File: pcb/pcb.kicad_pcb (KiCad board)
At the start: 2 copper layers, 56 x 58 mm, 20 parts, among them J1 Conn_01x03_Pin, J2 Screw_Terminal_01x06, J3 Barrel_Jack_Switch, J5 DE9_Plug, U1 74LS165, U2 LM7805_TO220

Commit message: New PDB files
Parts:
- removed J5: DE9_Plug, Connector_Dsub:DSUB-9_Female_Horizontal_P2.77x2.84mm_EdgePinOffset7.70mm_Housed_MountingHolesOffset9.12mm
- added J4: DE9_Plug_MountingHoles, Connector_Dsub:DSUB-9_Female_Horizontal_P2.77x2.84mm_EdgePinOffset7.70mm_Housed_MountingHolesOffset9.12mm, F.Cu at (190.7, 79.5)
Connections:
- J2 pad 4: VIDEO -> V_SYNC
- J2 pad 5: V_SYNC -> VIDEO
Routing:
- net VIDEO: track 29.0 -> 31.5 mm
- net PARALLEL_LOAD: track 34.3 -> 35.4 mm
- net V_SYNC: track 42.1 -> 43.1 mm
- net +5V: track 91.8 -> 91.2 mm
- net GND: vias 13 -> 18

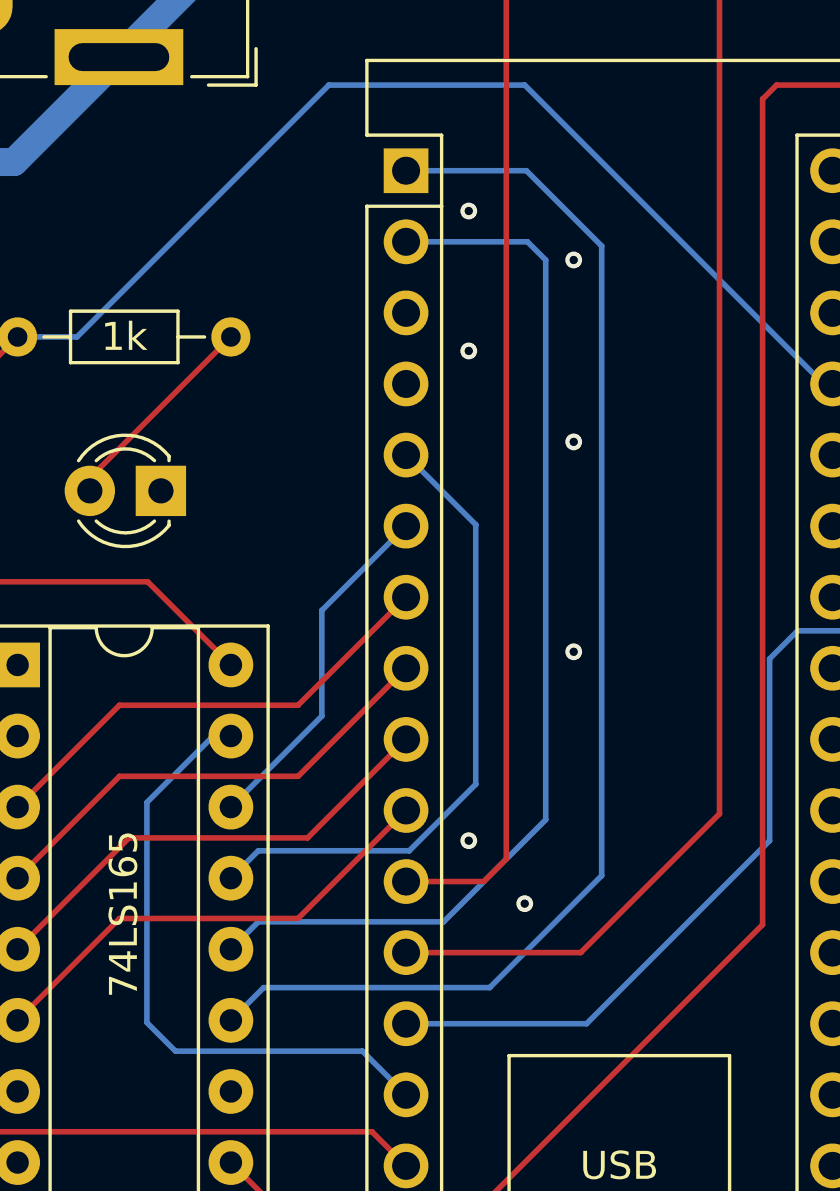
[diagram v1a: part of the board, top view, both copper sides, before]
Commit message: Fix backwards data lines
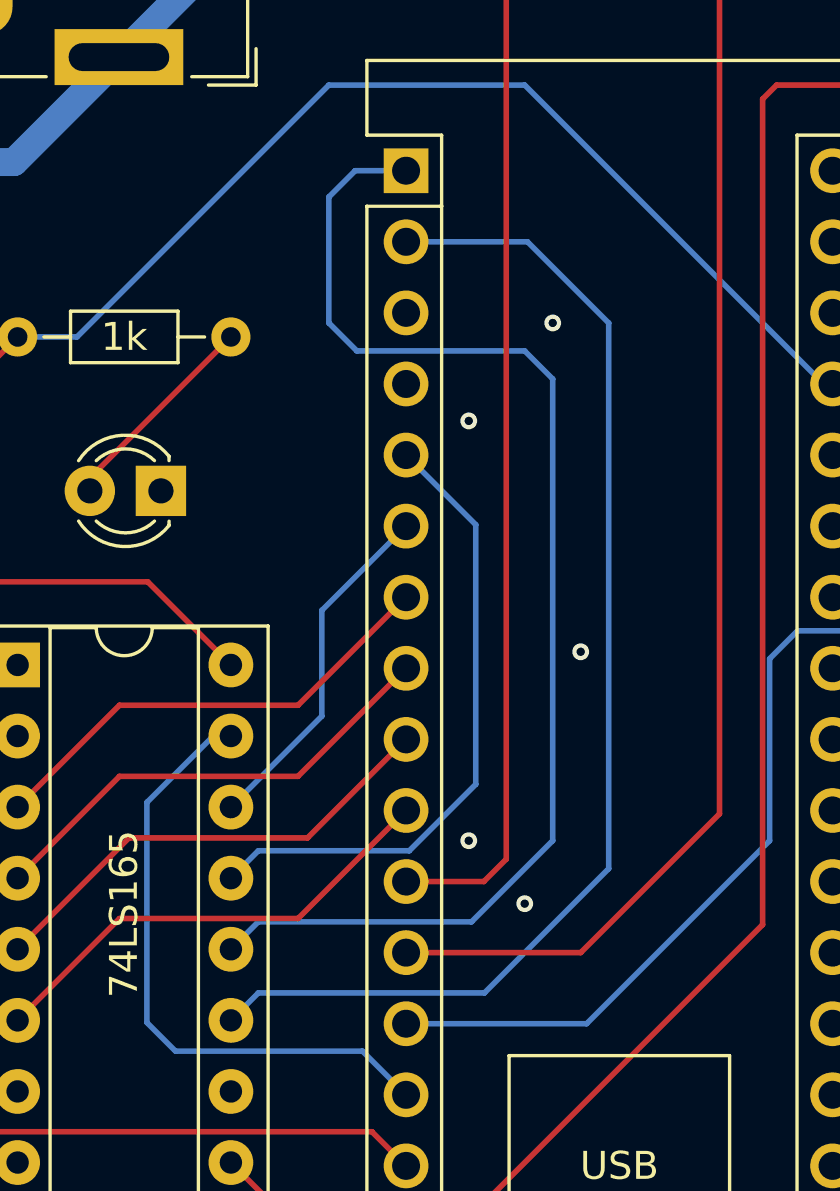
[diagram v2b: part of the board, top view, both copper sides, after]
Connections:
- A1 pad 1: DATA_7 -> DATA_6
- A1 pad 2: DATA_6 -> DATA_7
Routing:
- net DATA_6: track 38.4 -> 46.1 mm
- net DATA_7: track 46.0 -> 43.7 mm
- net GND: vias 18 -> 16
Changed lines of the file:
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@@
 			(layers "*.Cu" "*.Mask")
 			(remove_unused_layers no)
-			(net 23 "DATA_7")
+			(net 26 "DATA_6")
 			(pinfunction "D1/TX")
 			(pintype "bidirectional")
@@
 			(layers "*.Cu" "*.Mask")
 			(remove_unused_layers no)
-			(net 26 "DATA_6")
+			(net 23 "DATA_7")
 			(pinfunction "D0/RX")
 			(pintype "bidirectional")
@@
 	)
 	(via
-		(at 175.75 72.25)
-		(size 0.6)
-		(drill 0.3)
-		(layers "F.Cu" "B.Cu")
-		(free yes)
-		(net 10)
-	)
-	(via
-		(at 175.75 78.75)
+		(at 172 78)
 		(size 0.6)
 		(drill 0.3)
@@
 	)
 	(via
-		(at 172 75.5)
+		(at 176 86.25)
 		(size 0.6)
 		(drill 0.3)
@@
 	)
 	(via
-		(at 175.75 86.25)
+		(at 175 74.5)
 		(size 0.6)
 		(drill 0.3)
@@
 	)
 	(via
-		(at 172 70.5)
-		(size 0.6)
-		(drill 0.3)
-		(layers "F.Cu" "B.Cu")
-		(free yes)
-		(net 10)
-	)
-	(via
 		(at 172 93)
 		(size 0.6)
@@
 	)
 	(segment
-		(start 176.75 71.75)
-		(end 176.75 94.25)
+		(start 163.5 99.42)
+		(end 164.48 98.44)
 		(width 0.2)
 		(layer "B.Cu")
@@
 	)
 	(segment
-		(start 176.75 94.25)
-		(end 172.75 98.25)
+		(start 164.48 98.44)
+		(end 172.56 98.44)
 		(width 0.2)
 		(layer "B.Cu")
@@
 	)
 	(segment
-		(start 172.75 98.25)
-		(end 164.67 98.25)
+		(start 177 74.5)
+		(end 174.1 71.6)
 		(width 0.2)
 		(layer "B.Cu")
@@
 	)
 	(segment
-		(start 169.76 69.06)
-		(end 174.06 69.06)
+		(start 177 94)
+		(end 177 74.5)
 		(width 0.2)
 		(layer "B.Cu")
@@
 	)
 	(segment
-		(start 174.06 69.06)
-		(end 176.75 71.75)
+		(start 174.1 71.6)
+		(end 169.76 71.6)
 		(width 0.2)
 		(layer "B.Cu")
@@
 	)
 	(segment
-		(start 164.67 98.25)
-		(end 163.5 99.42)
+		(start 172.56 98.44)
+		(end 177 94)
 		(width 0.2)
 		(layer "B.Cu")
@@
 	)
 	(segment
-		(start 174.75 72.25)
-		(end 174.75 92.25)
+		(start 164.48 95.9)
+		(end 172.1 95.9)
 		(width 0.2)
 		(layer "B.Cu")
@@
 	)
 	(segment
-		(start 174.1 71.6)
-		(end 174.75 72.25)
+		(start 167 74.5)
+		(end 167 70)
 		(width 0.2)
 		(layer "B.Cu")
@@
 	)
 	(segment
-		(start 164.48 95.9)
-		(end 163.5 96.88)
+		(start 175 76.5)
+		(end 174 75.5)
 		(width 0.2)
 		(layer "B.Cu")
@@
 	)
 	(segment
-		(start 174.75 92.25)
-		(end 171.1 95.9)
+		(start 167.94 69.06)
+		(end 169.76 69.06)
 		(width 0.2)
 		(layer "B.Cu")
@@
 	)
 	(segment
-		(start 169.76 71.6)
-		(end 174.1 71.6)
+		(start 163.5 96.88)
+		(end 164.48 95.9)
 		(width 0.2)
 		(layer "B.Cu")
@@
 	)
 	(segment
-		(start 171.1 95.9)
-		(end 164.48 95.9)
+		(start 167 70)
+		(end 167.94 69.06)
+		(width 0.2)
+		(layer "B.Cu")
+		(net 26)
+	)
+	(segment
+		(start 172.1 95.9)
+		(end 175 93)
+		(width 0.2)
+		(layer "B.Cu")
+		(net 26)
+	)
+	(segment
+		(start 175 93)
+		(end 175 76.5)
+		(width 0.2)
+		(layer "B.Cu")
+		(net 26)
+	)
+	(segment
+		(start 168 75.5)
+		(end 167 74.5)
+		(width 0.2)
+		(layer "B.Cu")
+		(net 26)
+	)
+	(segment
+		(start 174 75.5)
+		(end 168 75.5)
 		(width 0.2)
 		(layer "B.Cu")
